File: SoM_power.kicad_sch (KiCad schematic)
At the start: 19 parts, among them J1 Hermaphroditic_Molex_203456-0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

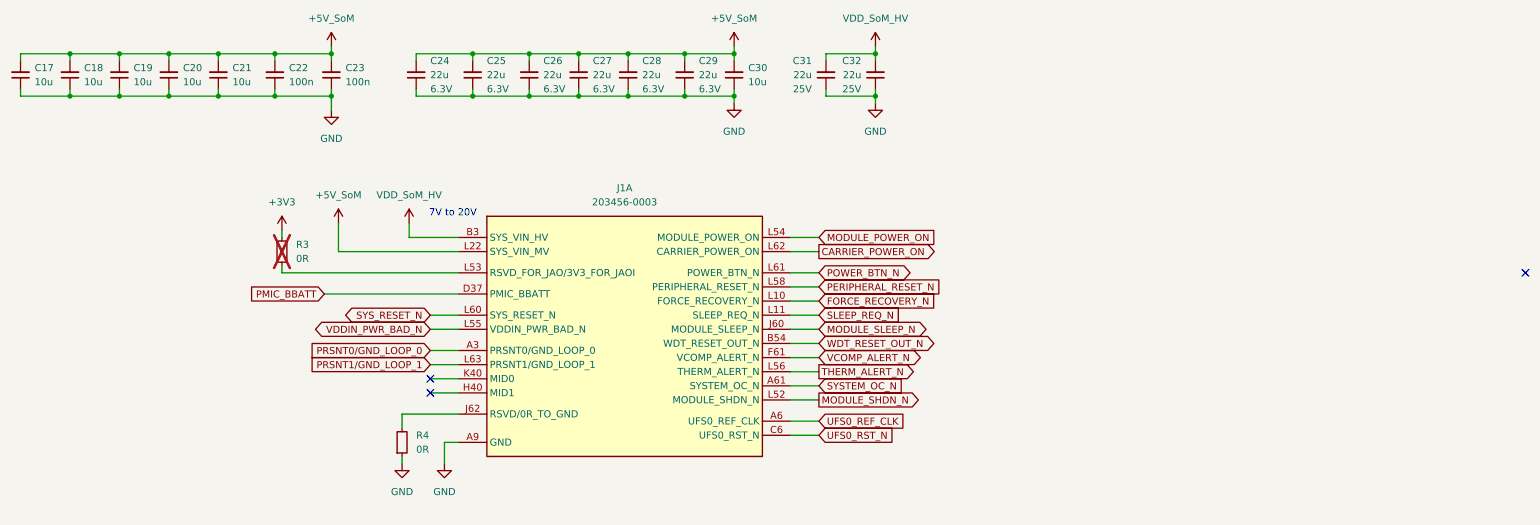
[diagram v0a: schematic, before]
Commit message: [#81782] Rebase power supply branch after review
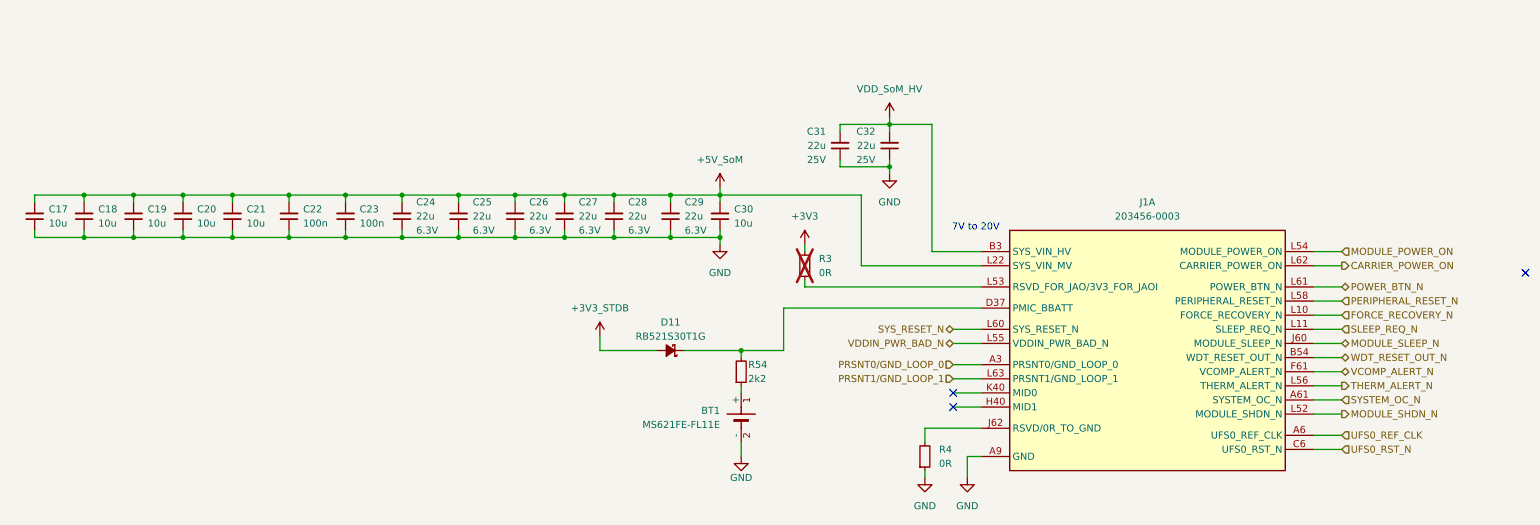
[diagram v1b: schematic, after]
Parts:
- added BT1: Battery_Holder_MS621FE-FL11E, antmicro-footprints:MS621FE-FL11E, symbol antmicroBatteryHoldersClipsContacts:Battery_Holder_MS621FE-FL11E
- added D11: RB521S30T1G, antmicro-footprints:SOD-523, symbol antmicroDiodesRectifiersSingle:RB521S30T1G
- added R54: R_2k2_0402, antmicro-footprints:R_0402_1005Metric, symbol antmicroResistors0402:R_2k2_0402
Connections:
- net GND: now also BT1.2 (-)
- net PMIC_BBATT: no longer names the net of J1.D37 (PMIC_BBATT)
- net PMIC_BBATT: now also D11.1 (C), R54.2
- net PRSNT0/GND_LOOP_0 renamed PRSNT0/GND_LOOP_0
- net PRSNT1/GND_LOOP_1 renamed PRSNT1/GND_LOOP_1
- new net: BT1.1 (+), R54.1
- new net +3V3_STDB: D11.2 (A)
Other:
- moved on the sheet: C17, C18, C19, C20, C21, C22, C23, C24, C25, C26, C27, C28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

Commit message: [#82757] Rename project to jetson-agx-thor-baseboard
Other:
- title: Jetson Orin AGX Baseboard -> Jetson AGX Thor Baseboard
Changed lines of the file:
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@@
 	(generator "eeschema")
 	(generator_version "9.0")
-	(paper "A4")
+	(paper "A3")
 	(title_block
-		(title "Jetson Orin AGX Baseboard")
+		(title "Jetson AGX Thor Baseboard")
 		(date "2025-08-11")
 		(rev "1.0.0")

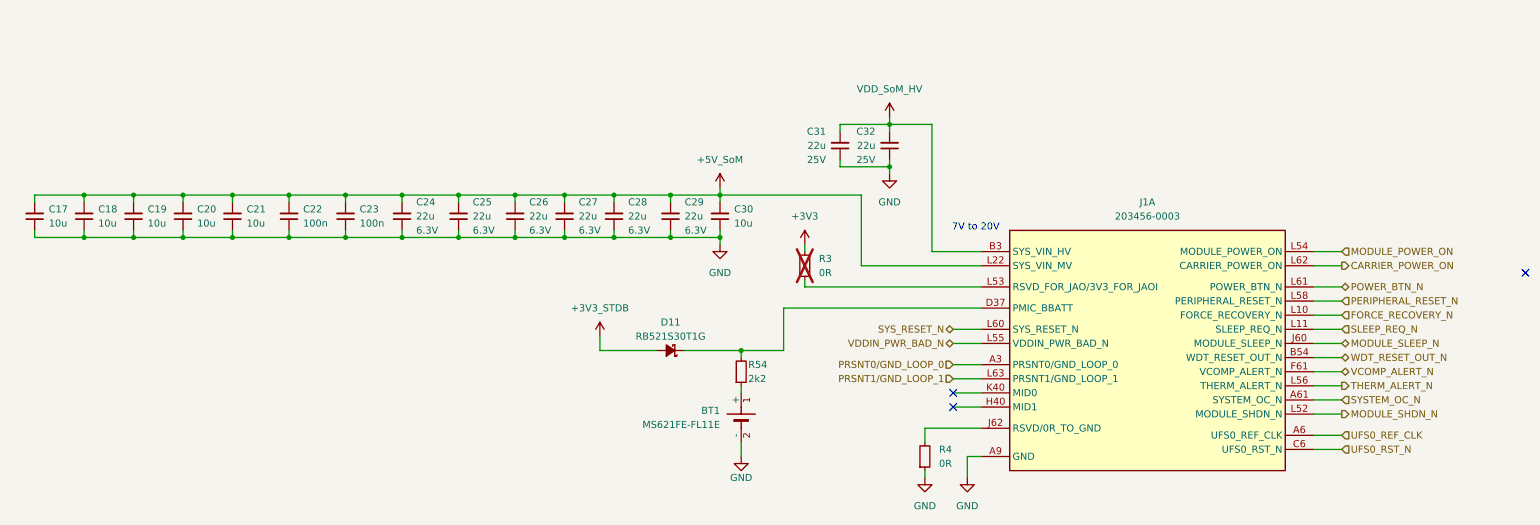
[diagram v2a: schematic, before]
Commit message: [#82757] Cleanup: reorganise page numbers and fix annotations
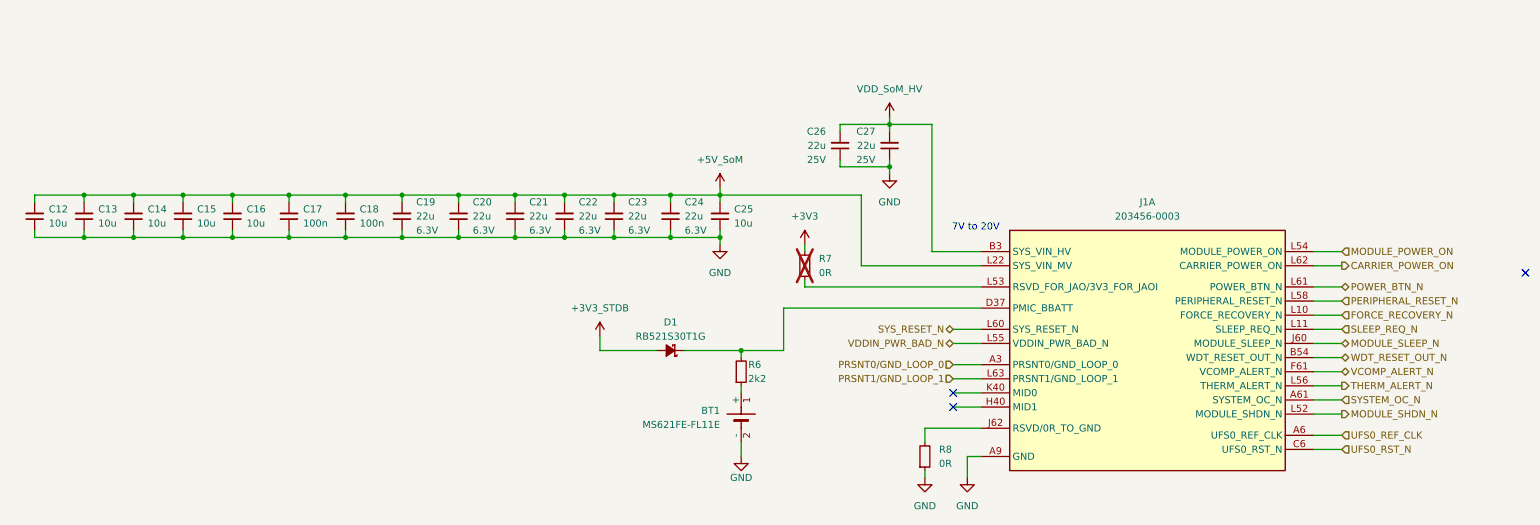
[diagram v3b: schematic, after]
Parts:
- renumbered C17 to C12, C18 to C13, C19 to C14, C20 to C15, C21 to C16, C22 to C17, C23 to C18, C24 to C19, C25 to C20, C26 to C21, C27 to C22, C28 to C23, C29 to C24, C30 to C25, C31 to C26, C32 to C27, D11 to D1, R54 to R6, R3 to R7, R4 to R8
